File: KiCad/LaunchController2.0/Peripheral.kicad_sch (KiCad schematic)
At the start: 20 parts, among them J11 CONN_AUDIO, J12 CONN_SPEAKER, J13 CONN_RS485, U10 ADM2582E, U11 24LC256, U8 MB85RQ8MX, U9 DFPlayer

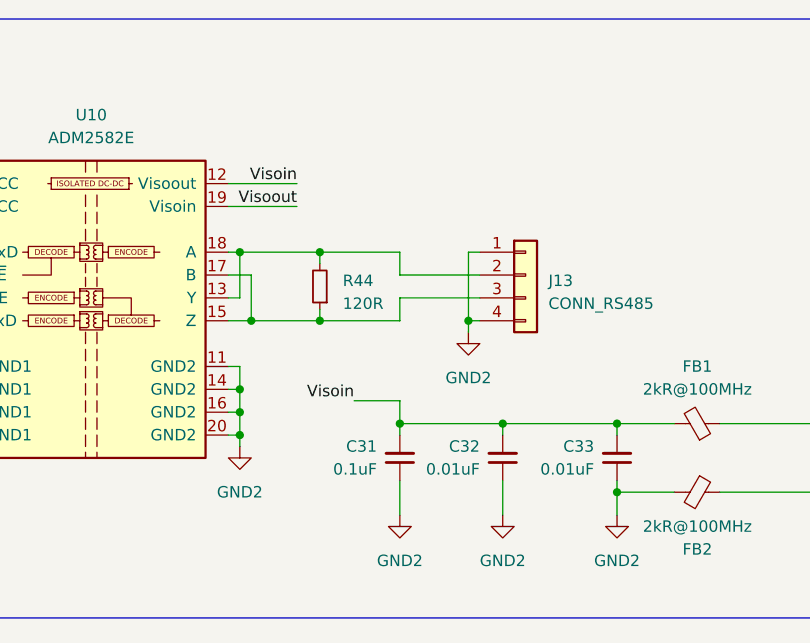
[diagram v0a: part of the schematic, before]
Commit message: 4層基板から2層基板へ仕様変更
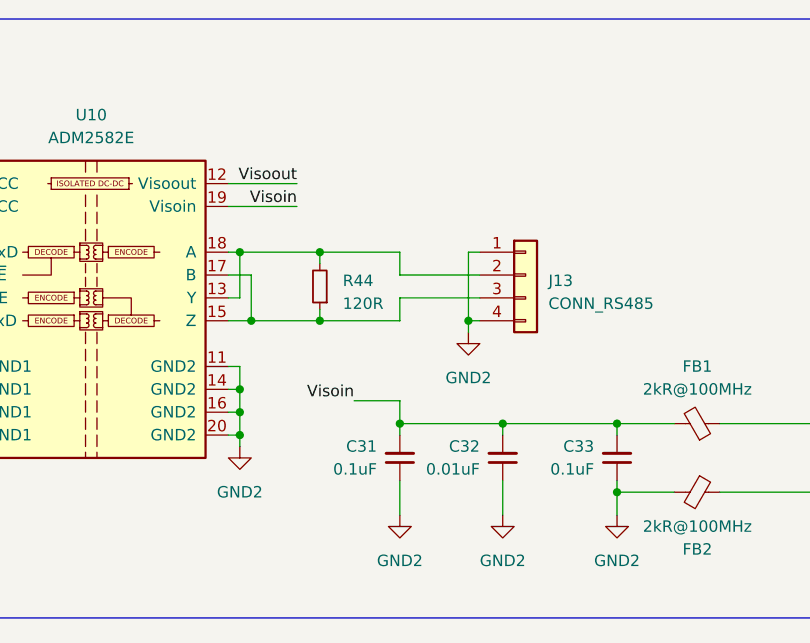
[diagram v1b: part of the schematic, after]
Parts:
- C33: value 0.01uF -> 0.1uF
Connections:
- net Visoin: now also U10.19 (Visoin); no longer U10.12 (Visoout)
- net Visoout: now also U10.12 (Visoout); no longer U10.19 (Visoin)
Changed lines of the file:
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@@
 	)
 	(label "Visoin"
+		(at 129.54 95.25 180)
+		(effects
+			(font
+				(size 1.27 1.27)
+			)
+			(justify right bottom)
+		)
+	)
+	(label "Visoout"
 		(at 129.54 92.71 180)
-		(effects
-			(font
-				(size 1.27 1.27)
-			)
-			(justify right bottom)
-		)
-	)
-	(label "Visoout"
-		(at 129.54 95.25 180)
 		(effects
 			(font
@@
 			)
 		)
-		(property "Value" "0.01uF"
+		(property "Value" "0.1uF"
 			(at 162.56 124.4535 0)
 			(effects
